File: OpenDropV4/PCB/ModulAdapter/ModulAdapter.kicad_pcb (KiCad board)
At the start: 2 copper layers, 100 x 69.5 mm, 14 parts, among them J1 Mini_Dimm_244, J2 Conn_01x24_Female, P1 ScrewPad2, P13 ScrewPad1, P14 ScrewPad2, P15 ScrewPad2, P17 ScrewPad1, P2 ScrewPad2, U2 HV507, U4 HV507

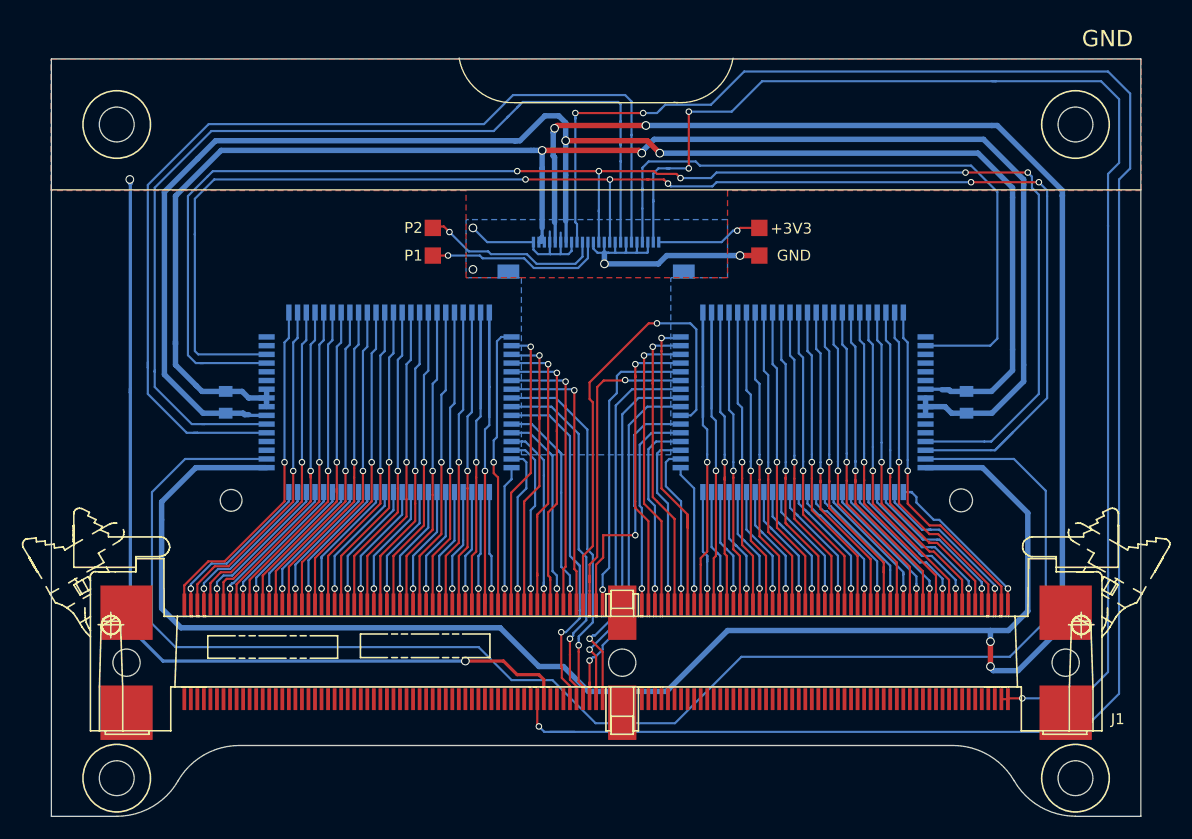
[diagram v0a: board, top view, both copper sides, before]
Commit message: Ready for second prototype round its not a synth
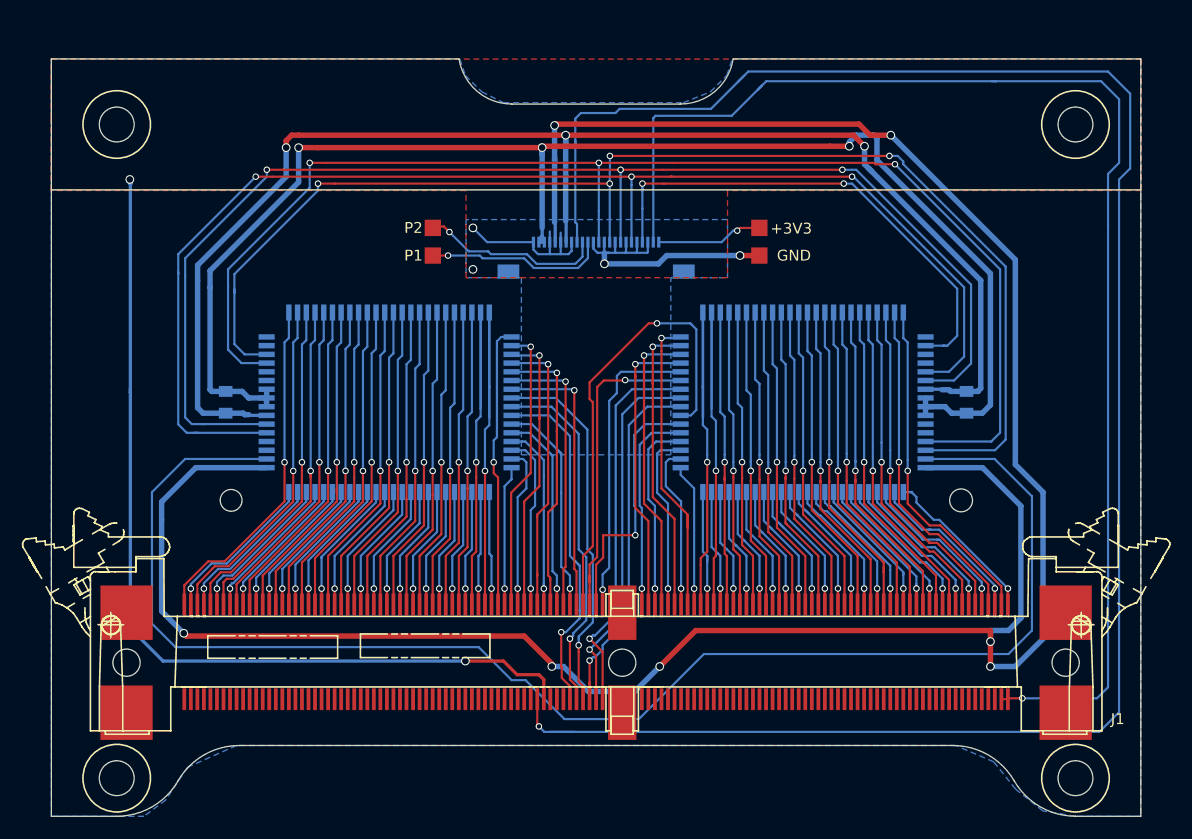
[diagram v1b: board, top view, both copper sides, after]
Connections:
- U4 pad 29: (no net) -> BL_C
- U4 pad 30: (no net) -> POL_C
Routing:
- net POL_C: track 90.0 -> 121.6 mm, vias 0 -> 3
- net BL_C: track 93.5 -> 120.3 mm, vias 0 -> 3
- net LE_C: track 140.9 -> 120.5 mm, vias 5 -> 4
- net CLK_C: track 140.5 -> 121.3 mm, vias 5 -> 3
- net VDD_C: track 147.4 -> 130.7 mm, vias 2 -> 3
- net GND_C: track 149.2 -> 133.9 mm, vias 2 -> 3
- net DI_C: track 61.6 -> 46.4 mm, vias 0 -> 2
- net V_HV_C: track 238.3 -> 231.0 mm, vias 4 -> 7
- net Net-(U2-Pad26): track 137.8 -> 135.1 mm
- net SENS_PAD: track 180.9 -> 182.5 mm, vias 3 -> 1
- net V_GND: track 121.5 -> 122.3 mm, vias 3 -> 1
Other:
- outline, holes or cut-outs redrawn
- board text added: "Modul Adapter V4.0"
- board text removed: "BL"
- board text removed: "CLK"
- board text removed: "DIO"
- board text removed: "GND"
- board text removed: "HV"
- board text removed: "LE"
- board text removed: "Modul Adapter V1.1"
- board text removed: "Module Adapter V1.0 2019"
- board text removed: "VDD"
- board text removed: "www.gaudi.ch/OpenDrop"
